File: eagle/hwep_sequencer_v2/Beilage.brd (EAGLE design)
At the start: 256.5 x 87.6 mm, 175 parts, among them X1 ESP32-AZDEL

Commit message: Board: Bedruck Formatiert
Board Optimiert und Layer:
Names
Values
Formatiert
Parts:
- moved R14 6.35 mm to (158.8, 55.9), turned to 90 degrees
- moved C15 4.07 mm to (220.3, 71.1)
- moved R49 2.84 mm to (171.4, 44.5), turned to 270 degrees
- moved R18 1.27 mm to (238.8, 26.7)
- moved R20 1.27 mm to (243.8, 26.7)
- moved R35 1.27 mm to (212.1, 49.5)
- moved R36 1.27 mm to (212.1, 44.5)
- moved R37 1.27 mm to (212.1, 57.1)
- moved R38 1.27 mm to (212.1, 52.1)
- moved R39 1.27 mm to (212.1, 47.0)
- moved R40 1.27 mm to (212.1, 62.2)
- moved R41 1.27 mm to (212.1, 54.6)
- moved R42 1.27 mm to (212.1, 59.7)
- moved R43 1.27 mm to (207.0, 43.2)
- moved R19 1.27 mm to (241.3, 26.7)
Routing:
- net GND: track 62.3 -> 76.5 mm, vias 17 -> 16
- net 7SEG_D: track 20.8 -> 24.6 mm
- net PAUSE_CNT: track 16.6 -> 12.9 mm, vias 1 -> 0
- net +3V3: track 1202.1 -> 1199.7 mm
- net CLRR: track 35.8 -> 34.2 mm
- net RESET_CNT: track 58.5 -> 59.9 mm
- net 7SEG_B: track 16.5 -> 17.8 mm
- net N$80: track 35.1 -> 33.9 mm
- net N$78: track 47.4 -> 46.1 mm
- net N$7: track 27.5 -> 26.2 mm
- net N$56: track 35.1 -> 33.9 mm
- net N$37: track 27.5 -> 26.2 mm
- net N$36: track 27.5 -> 26.2 mm
- net N$35: track 35.1 -> 33.9 mm
- net EC11_SW: track 58.4 -> 59.6 mm
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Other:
- board text added: "3x"

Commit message: Board Prototyp Fertiggestellt
Fehlende Entkoppel-Kondensatoren eingefügt
Bestückungsdruck überarbeitet und Formatiert
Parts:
- added C21, C22, C25, C26: 1u, rcl_GruS:C0805
- added C23, C24, C27, C28: 100n, rcl_GruS:C0805
- C13, C14, C17, C18: value 1u -> 100n
- R13: value 10k -> 56k; device rcl_GruS:P160L -> rcl_GruS:R0805
- R2: device rcl_GruS:R0805 -> rcl_GruS:P160L
- R20: value 56k -> 10k
- R6: value 10k -> 330R; device rcl_GruS:P160L -> rcl_GruS:R0805
- R8: value 330R -> 1M
- R9: value 1M -> 10k; device rcl_GruS:R0805 -> rcl_GruS:P160L
- moved R2 229.2 mm to (11.4, 8.89), turned to 0 degrees
- moved R8 161.3 mm to (172.7, 67.3)
- moved R7 161.3 mm to (11.4, 71.1), turned to 180 degrees
- moved R6 118.7 mm to (172.7, 72.4)
- moved R17 108.7 mm to (238.8, 26.7), turned to 90 degrees
- moved R9 99.1 mm to (92.7, 8.89), turned to 0 degrees
- moved R1 76.9 mm to (234.9, 59.7)
- moved R20 75.2 mm to (168.9, 20.3), turned to 180 degrees
- moved C15 73.4 mm to (194.3, 2.54), flipped to the bottom, turned to 0 degrees
- moved C14 71.2 mm to (208.3, 7.62), flipped to the bottom, turned to 315 degrees
- moved C16 71.0 mm to (180.3, 7.62), flipped to the bottom, turned to 45 degrees
- moved C17 57.4 mm to (175.3, 21.6), flipped to the bottom, turned to 90 degrees
- moved C18 57.2 mm to (180.3, 35.6), flipped to the bottom, turned to 135 degrees
- moved C13 52.1 mm to (213.4, 21.6), flipped to the bottom, turned to 270 degrees
- moved R13 47.3 mm to (158.8, 55.9), flipped to the bottom, turned to 90 degrees
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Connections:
- net +3V3: now also C21.1, C22.1, C23.1, C24.1, C25.1, C26.1, C27.1, C28.1, R17.2, R2.3, R9.3; no longer C13.1, C14.1, C15.1, C16.1, C17.1, C18.1, C19.1, C20.1, R13.3, R2.2, R6.3
- net +5V: now also C13.1, C14.1, C15.1, C16.1, C17.1, C18.1, C19.1, C20.1
- net 088S052_!CS!: now also R20.1; no longer R1.1
- net 23S08_!CS: now also R1.1; no longer R2.1
- net ADC0: now also R2.2; no longer R3.2
- net ADC1: now also R3.2; no longer R4.2
- net ADC2: now also R4.2; no longer R5.2
- net ADC3: now also R5.2; no longer R6.2
- net ADC4: now also R9.2; no longer R10.2
- net ADC5: now also R10.2; no longer R11.2
- net ADC6: now also R11.2; no longer R12.2
- net ADC7: now also R12.2; no longer R13.2
- net CLRR: now also R16.2; no longer R17.2
- net EC11_A: now also R17.1; no longer R18.1
- net EC11_B: now also R18.1; no longer R19.1
- net EC11_SW: now also R19.1; no longer R20.1
- net EVENT: now also R15.2, R8.2; no longer R16.2, R9.2
- net GND: now also C21.2, C22.2, C23.2, C24.2, C25.2, C26.2, C27.2, C28.2, R2.1, R7.1; no longer R17.1, R6.1
- net N$58: now also R6.2; no longer R7.2
- net N$60: now also R6.1; no longer R7.1
- net N$9: now also R7.2; no longer R8.2
- net PAUSE_CNT: now also R13.2; no longer R14.2
- net RESET_CNT: now also R14.2; no longer R15.2
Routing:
- net GND: track 76.5 -> 104.7 mm
- net +5V: track 160.6 -> 187.0 mm
- net PL_DIN: track 48.9 -> 50.1 mm
- net +3V3: track 1199.7 -> 1198.5 mm
- net N$8: track 3.37 -> 2.87 mm

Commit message: RGB Ring now in SMD
SMD RGB LEDS WS2812 used because of availability
PSU Buck Converter 12v to 5v still to be added to the schematic
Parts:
- added C29, C30: 1u, rcl_GruS:C0805
- added C31, C32: 100n, rcl_GruS:C0805
- added H46, H47, H48, H49: ge, led_GruS:LED5MM
- C21, C22: value 1u -> 100n
- H10, H3, H4, H5, H6, H7, H8, H9: value PL9823-F5 -> WS2812B; device led_GruS:LED-PL9823-F5 -> led_GruS:WS2812B
- H11, H12, H13: value (none) -> WS2812B; device display_GruS:HDSP-E -> led_GruS:WS2812B
- H14: value rt -> WS2812B; device led_GruS:CHIPLED_1206 -> led_GruS:WS2812B
- H15, H16, H17: value rt -> (none); device led_GruS:CHIPLED_1206 -> display_GruS:HDSP-E
- H30, H31, H32, H33: value gn -> rt; device led_GruS:LED5MM -> led_GruS:CHIPLED_1206
- H38, H39, H40, H41: value ge -> gn
- moved H2 225.7 mm to (236.2, 88.9)
- moved R7 225.3 mm to (236.2, 86.4)
- moved H30 200.5 mm to (205.7, 83.8)
- moved H31 183.3 mm to (208.3, 83.8)
- moved C25 173.0 mm to (212.1, 80.0), turned to 0 degrees
- moved H32 166.3 mm to (210.8, 83.8)
- moved H33 149.4 mm to (213.4, 83.8)
- moved C26 146.4 mm to (181.6, 80.0)
- moved H34 81.5 mm to (11.4, 40.6)
- moved H35 81.5 mm to (31.8, 40.6)
- moved H36 81.5 mm to (52.1, 40.6)
- moved H42 81.5 mm to (11.4, 52.1)
- moved H43 81.5 mm to (31.8, 52.1)
- moved H44 81.5 mm to (52.1, 52.1)
- moved H37 81.5 mm to (72.4, 40.6)
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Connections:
- new net N$67: H12.2, H4.4
- new net N$69: H5.2, H8.4
- new net N$71: H11.4, H8.2
- new net N$72: H11.2, H14.4
- net +3V3: now also C29.1, C30.1, C31.1, C32.1, H46.A, H47.A, H48.A, H49.A; no longer C21.1, C22.1, C23.1, C24.1, H14.A, H15.A, H16.A, H17.A
- net +5V: now also C21.1, C22.1, C23.1, C24.1, H10.1, H11.1, H12.1, H13.1, H14.1, H3.1, H4.1, H5.1, H6.1, H7.1, H8.1, H9.1; no longer H10.2, H3.2, H4.2, H5.2, H6.2, H7.2, H8.2, H9.2
- net GND: now also C29.2, C30.2, C31.2, C32.2, H11.3, H12.3, H13.3, H14.3
- net N$10: now also H18.C; no longer H14.C
- net N$11: now also H19.C; no longer H15.C
- net N$12: now also H20.C; no longer H16.C
- net N$13: now also H21.C; no longer H17.C
- net N$20: now also H22.C; no longer H18.C
- net N$21: now also H23.C; no longer H19.C
- net N$22: now also H24.C; no longer H20.C
- net N$23: now also H25.C; no longer H21.C
- net N$25: now also H26.C; no longer H22.C
- net N$26: now also H27.C; no longer H23.C
- net N$27: now also H28.C; no longer H24.C
- net N$28: now also H29.C; no longer H25.C
- net N$29: now also H30.C; no longer H26.C
- net N$30: now also H31.C; no longer H27.C
- net N$31: now also H32.C; no longer H28.C
- net N$32: now also H33.C; no longer H29.C
- net N$33: now also H15.G, H16.G, H17.G; no longer H11.G, H12.G, H13.G
- net N$35: now also H15.F, H16.F, H17.F; no longer H11.F, H12.F, H13.F
- net N$36: now also H15.A, H16.A, H17.A; no longer H11.A, H12.A, H13.A
- net N$37: now also H15.B, H16.B, H17.B; no longer H11.B, H12.B, H13.B
- net N$38: now also H34.K; no longer H30.K
- net N$39: now also H35.K; no longer H31.K
- net N$4: now also H13.2, H5.4; no longer H4.1, H9.4
- net N$40: now also H36.K; no longer H32.K
- net N$41: now also H37.K; no longer H33.K
- net N$42: now also H38.K; no longer H34.K
- net N$43: now also H39.K; no longer H35.K
- net N$44: now also H40.K; no longer H36.K
- net N$45: now also H41.K; no longer H37.K
- net N$46: now also H42.K; no longer H38.K
- net N$47: now also H43.K; no longer H39.K
- net N$48: now also H44.K; no longer H40.K
- net N$49: now also H45.K; no longer H41.K
- net N$50: now also H46.K; no longer H42.K
- net N$51: now also H47.K; no longer H43.K
- net N$52: now also H48.K; no longer H44.K
- net N$53: now also H49.K; no longer H45.K
- net N$55: now also H15.CC1, H15.CC2; no longer H11.CC1, H11.CC2
- net N$56: now also H15.D, H16.D, H17.D; no longer H11.D, H12.D, H13.D
- net N$57: now also H4.2, H7.4; no longer H4.4, H6.1
- net N$59: now also H10.4, H7.2; no longer H6.4, H8.1
- net N$63: now also H10.2, H13.4; no longer H10.1, H8.4
- net N$64: now also H16.CC1, H16.CC2; no longer H12.CC1, H12.CC2
- net N$65: now also H17.CC1, H17.CC2; no longer H13.CC1, H13.CC2
- net N$68: now also H3.2, H6.4; no longer H3.4, H5.1
- net N$7: now also H15.DP, H16.DP, H17.DP; no longer H11.DP, H12.DP, H13.DP
- net N$70: now also H6.2, H9.4; no longer H5.4, H7.1
- net N$73: now also H12.4, H9.2; no longer H7.4, H9.1
- net N$78: now also H15.C, H16.C, H17.C; no longer H11.C, H12.C, H13.C
- net N$8: now also H3.4; no longer H3.1
- net N$80: now also H15.E, H16.E, H17.E; no longer H11.E, H12.E, H13.E
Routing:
- net PL_DIN: track 50.1 -> 3.79 mm
- net N$8: track 2.87 -> 32.5 mm
- net GND: track 104.7 -> 75.8 mm
- net +3V3: track 1198.5 -> 1223.8 mm, vias 15 -> 14
- net +5V: track 187.0 -> 208.5 mm, vias 0 -> 1
- net 088S052_!CS!: track 70.4 -> 77.4 mm, vias 2 -> 0
- net N$69: track 0.00 -> 5.87 mm
- net N$71: track 0.00 -> 5.84 mm
- net N$67: track 0.00 -> 5.84 mm
- net SCK: track 162.9 -> 168.6 mm
- net N$72: track 0.00 -> 5.57 mm
- net EC11_SW: track 59.6 -> 55.6 mm, vias 1 -> 0
- net MISO: track 85.3 -> 89.2 mm
- net N$9: track 2.87 -> 0.00 mm
- net ADC4: track 74.9 -> 72.4 mm
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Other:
- board size 256.5 x 87.6 mm -> 251.5 x 94 mm

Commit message: Major Prescaler Update
Optimized Prescaler:
Now Fully Software side.
Inputs are priority encoded and put on MCP23S08 free input pins.
Issues:
Analog Reference Voltage Needed?
Dedicated PSU / Voltage converter
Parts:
- removed C31, C32: 100n, rcl_GruS:C0805
- removed D14, D16: 74AHC1G04DBV, 74xx_GruS:SOT23-5
- removed D15: STP16CP05TTR, ic_GruS:TSSOP24
- removed R14, R18: 56k, rcl_GruS:R0805
- removed R2, R9: 10k, rcl_GruS:P160L
- removed R35, R36, R37, R38, R39, R40, R41, R42: 100R, rcl_GruS:R0805
- removed R43, R44, R45: 100k, rcl_GruS:R0805
- removed R46, R48: 10k, rcl_GruS:R0805
- removed R47, R49: 2k7, rcl_GruS:R0805
- removed V10, V11, V12, V13, V14, V15, V16, V17, V18, V19, V20, V21, V22, V23, V24, V25, V4, V5, V6, V7, V8, V9: 1N4148-7, diode_GruS:DO35-7
- removed V26, V27, V28: NTR4003, mfet_GruS:SOT23
- C10, C11, C25, C26, C29, C30: value 1u -> 100n
- C23, C24, C27, C28: value 100n -> 1u
- C4, C5: value 100n -> 10n
- C6, C7: value 10n -> 100n
- D1: value 74AHC138N -> MCP23S08SO; device 74xx_GruS:DIP16 -> ic_GruS:SO18W
- D10: value 74HC73N -> STP16CP05TTR; device 74xx_GruS:DIP14 -> ic_GruS:TSSOP24
- D11: value 74HC151N -> 74AHC1G04DBV; device 74xx_GruS:DIP16 -> 74xx_GruS:SOT23-5
- D12: value 74AHCT1G125DBV -> STP16CP05TTR; device 74xx_GruS:SOT23-5 -> ic_GruS:TSSOP24
- D13: value STP16CP05TTR -> 74AHC1G04DBV; device ic_GruS:TSSOP24 -> 74xx_GruS:SOT23-5
- D2: value MCP23S08SO -> 74AHC1G125DBV; device ic_GruS:SO18W -> 74xx_GruS:SOT23-5
- D4: value 74AHC1G125DBV -> 74AHC138N; device 74xx_GruS:SOT23-5 -> 74xx_GruS:DIP16
- D6: value 74HC151N -> 74HC148N
- D7: value 74HC193D -> 74HC148N; device 74xx_GruS:SO16 -> 74xx_GruS:DIP16
- D8: value 74HC73N -> 74HC00N
- D9: value 74HC73N -> 74AHCT1G125DBV; device 74xx_GruS:DIP14 -> 74xx_GruS:SOT23-5
- R13: value 56k -> 10k; device rcl_GruS:R0805 -> rcl_GruS:P160L
- R15, R16, R17, R19: value 56k -> 10k
- R20: value 10k -> 100R
- R21, R22, R23, R24, R25, R26, R27: value 100k -> 100R
- R31, R33: value 100k -> 10k
- R32, R34: value 100k -> 2k7
- R6: value 330R -> 10k; device rcl_GruS:R0805 -> rcl_GruS:P160L
- R7: value 330R -> 1k
- R8: value 1M -> 1k
- S14: value (none) -> EC11E09244AQ; device switch_GruS:B3F-10XX -> switch_GruS:EC11
- S15: value EC11E09244AQ -> (none); device switch_GruS:EC11 -> switch_GruS:B3F-10XX
- V2, V3: value 1N4148-7 -> NTR4003; device diode_GruS:DO35-7 -> mfet_GruS:SOT23
- moved R32 205.8 mm to (227.3, 78.7), turned to 0 degrees
- moved R21 201.2 mm to (212.1, 50.8), turned to 180 degrees
- moved R28 198.6 mm to (207.0, 49.5), turned to 0 degrees
- moved R22 188.0 mm to (212.1, 63.5), turned to 180 degrees
- moved R27 185.4 mm to (212.1, 66.0), turned to 180 degrees
- moved C27 179.6 mm to (42.5, 52.1)
- moved R29 177.3 mm to (198.1, 49.5), turned to 0 degrees
- moved R31 176.5 mm to (221.0, 83.8), flipped to the top
- moved C28 173.5 mm to (42.5, 40.6), turned to 180 degrees
- moved R23 170.4 mm to (212.1, 58.4), turned to 180 degrees
- moved R24 168.1 mm to (212.1, 53.3), turned to 180 degrees
- moved R30 145.1 mm to (188.0, 49.5), turned to 0 degrees
- moved R34 133.7 mm to (171.4, 50.8), flipped to the top
- moved D9 130.8 mm to (242.6, 21.6)
- moved R25 129.6 mm to (212.1, 68.6), turned to 180 degrees
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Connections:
- removed net !CS!_C: D1.3, X1.36
- removed net BPM_DIV_Q0: D6.11, D9.9
- removed net BPM_DIV_Q1: D10.12, D6.10
- removed net BPM_DIV_Q2: D10.9, D6.9
- removed net GATE_DIV_Q0: D11.11, D8.9
- removed net GATE_DIV_Q1: D11.10, D8.12
- removed net GATE_DIV_Q2: D11.9, D9.12
- removed net N$14: D8.3, R25.2, V6.C, V9.C
- removed net N$15: D9.10, R30.2, V14.C, V16.C
- removed net N$16: D10.10, R34.2, V23.C, V24.C, V25.C
- removed net N$17: D10.7, R33.2, V22.C
- removed net N$18: D10.14, R31.2, V19.C, V20.C
- removed net N$19: D9.7, R29.2, V15.C, V17.C
- removed net N$2: D8.10, R23.2, V2.C, V4.C
- removed net N$3: D8.14, R24.2, V7.C, V8.C
- removed net N$34: D10.3, R32.2, V18.C, V21.C
- removed net N$5: D8.7, R22.2, V3.C, V5.C
- removed net N$6: D9.3, R27.2, V11.C, V12.C, V13.C
- removed net N$60: R6.1, V1.3
- removed net PS_BPM: D6.5, X1.6
- removed net PS_GATE: D11.5, X1.5
- removed net Q0: D11.3, D6.3, D7.3
- removed net Q1: D11.2, D6.2, D7.2
- removed net Q2: D11.1, D6.1, D7.6
- removed net Q3: D11.15, D6.15, D7.7
- removed net SRC_BPM: D10.1, D10.5, D11.4, D6.4, D7.4, D8.1, D8.5, D9.1, D9.5, X1.7
- new net AGND: C6.2, D5.3, R10.1, R11.1, R12.1, R13.1, R3.1, R4.1, R5.1, R6.1
- new net GS_B: D6.14, D8.13
- new net GS_G: D7.14, D8.12
- new net PS0: D1.14, D8.3
- new net PS1: D1.15, D8.6
- new net PS2: D1.16, D8.8
- new net PS3: D1.17, D8.11
- new net PS_B0: D6.9, D8.1
- new net PS_B1: D6.7, D8.4
- new net PS_B2: D6.6, D8.10
- new net PS_G0: D7.9, D8.2
- new net PS_G1: D7.7, D8.5
- new net PS_G2: D7.6, D8.9
- net !CS!_A: now also D4.1; no longer D1.1
- net !CS!_B: now also D4.2; no longer D1.2
- net +3V3: now also C23.1, C24.1, C6.1, C7.1, D1.18, D10.24, D11.5, D12.24, D13.5, D2.5, D4.16, D4.6, D6.10, D6.11, D6.12, D7.10, D7.12, D8.14, R13.3, R15.2, R16.2, R31.2, R33.2, R6.3, S14.C1; no longer C10.1, C11.1, C31.1, C32.1, C4.1, C5.1, D1.16, D10.4, D11.16, D13.24, D14.5, D15.24, D16.5, D2.18, D2.6, D4.5, D7.5, D8.4, D9.4, H1.A, R18.2, R2.3, R20.2, R21.2, R28.2, R46.2, R48.2, R9.3, S10.2, S11.1, S12.1, S13.2, S14.1, S2.1, S3.1, S4.1, S5.1, S7.2, S8.2, S9.2
- net +5V: now also C10.1, C11.1, D9.5; no longer C23.1, C24.1, D12.5
- net 088S052_!CS!: now also D4.12, R19.1; no longer D1.12, R20.1
- net 23S08_!CS: now also D1.7, D2.1, D4.15; no longer D1.15, D2.7, D4.1
- net 7SEG_A: now also R27.2; no longer R42.2
- net 7SEG_B: now also R26.2; no longer R41.2
- net 7SEG_C: now also R25.2; no longer R40.2
- net 7SEG_CE: now also R30.2, V3.1; no longer R45.2, V28.1
- net 7SEG_CH: now also R28.2, V1.1; no longer R43.2, V26.1
- net 7SEG_CZ: now also R29.2, V2.1; no longer R44.2, V27.1
- net 7SEG_D: now also R24.2; no longer R39.2
- net 7SEG_DP: now also R20.2; no longer R35.2
- net 7SEG_E: now also R23.2; no longer R38.2
- net 7SEG_F: now also R22.2; no longer R37.2
- net 7SEG_G: now also R21.2; no longer R36.2
- net ADC0: now also R3.2; no longer R2.2
- net ADC1: now also R4.2; no longer R3.2
- net ADC2: now also R5.2; no longer R4.2
- net ADC3: now also R6.2; no longer R5.2
- net ADC4: now also R10.2; no longer R9.2
- net ADC5: now also R11.2; no longer R10.2
- net ADC6: now also R12.2; no longer R11.2
- net ADC7: now also R13.2; no longer R12.2
- net CLRR: now also D1.11; no longer D2.11, R16.2
- net EC11_A: now also C4.1, R15.1, S14.A1; no longer C6.1, R17.1, S15.A1
- net EC11_B: now also C5.1, R16.1, S14.B1; no longer C7.1, R18.1, S15.B1
- net EC11_SW: now also R17.1, S14.E1; no longer R19.1, S15.E1
- net EVENT: now also D1.10, H1.A, S12.4; no longer D2.10, R15.2, R8.2, S13.4, V1.1
- net GND: now also D1.9, D10.1, D10.21, D11.3, D12.21, D13.3, D2.3, D4.4, D4.5, D4.8, D6.5, D8.7, D9.1, D9.3, R28.1, S1.2, S10.1, S10.2, S11.1, S11.2, S12.1, S12.2, S13.1, S13.2, S14.D1, S14.MH1, S14.MH2, S15.1, S15.2, S2.1, S2.2, S3.1, S3.2, S4.1, S4.2, S5.1, S5.2, S6.2, S7.1, S7.2, S8.1, S8.2, S9.1, S9.2, V2.2, V3.2; no longer C31.2, C32.2, C6.2, D1.8, D10.11, D11.7, D11.8, D12.3, D13.1, D13.21, D14.3, D15.1, D15.21, D16.3, D2.4, D2.5, D2.9, D4.3, D5.3, D6.7, D7.14, D8.11, D9.11, R10.1, R11.1, R12.1, R13.1, R14.1, R15.1, R16.1, R2.1, R22.1, R23.1, R24.1, R25.1, R26.1, R27.1, R3.1, R31.1, R33.1, R4.1, R43.1, R44.1, R45.1, R47.1, R49.1, R5.1, R9.1, S15.C1, S15.D1, S15.MH1, S15.MH2, V26.2, V27.2, V28.2
- net MISO: now also D2.4; no longer D4.4
- net MOSI: now also D10.2, D12.2; no longer D13.2, D15.2
- net N$1: now also D6.15, D7.5; no longer D9.14, R26.2, V10.C
- net N$10: now also D10.5; no longer D13.5
- net N$11: now also D10.6; no longer D13.6
- net N$12: now also D10.7; no longer D13.7
- net N$13: now also D10.8; no longer D13.8
- net N$20: now also D10.9; no longer D13.9
- net N$21: now also D10.10; no longer D13.10
- net N$22: now also D10.11; no longer D13.11
- net N$23: now also D10.12; no longer D13.12
- net N$24: now also D10.23, R32.2; no longer D13.23, R47.2
- net N$25: now also D10.13; no longer D13.13
- net N$26: now also D10.14; no longer D13.14
- net N$27: now also D10.15; no longer D13.15
- net N$28: now also D10.16; no longer D13.16
- net N$29: now also D10.17; no longer D13.17
- net N$30: now also D10.18; no longer D13.18
- net N$31: now also D10.19; no longer D13.19
- net N$32: now also D10.20; no longer D13.20
- net N$33: now also R21.1; no longer R36.1
- net N$35: now also R22.1; no longer R37.1
- net N$36: now also R27.1; no longer R42.1
- net N$37: now also R26.1; no longer R41.1
- net N$38: now also D12.5; no longer D15.5
- net N$39: now also D12.6; no longer D15.6
- net N$40: now also D12.7; no longer D15.7
- net N$41: now also D12.8; no longer D15.8
- net N$42: now also D12.9; no longer D15.9
- net N$43: now also D12.10; no longer D15.10
- net N$44: now also D12.11; no longer D15.11
- net N$45: now also D12.12; no longer D15.12
- net N$46: now also D12.13; no longer D15.13
- net N$47: now also D12.14; no longer D15.14
- net N$48: now also D12.15; no longer D15.15
- net N$49: now also D12.16; no longer D15.16
- net N$50: now also D12.17; no longer D15.17
- net N$51: now also D12.18; no longer D15.18
- net N$52: now also D12.19; no longer D15.19
- net N$53: now also D12.20; no longer D15.20
- net N$54: now also D12.23, R34.2; no longer D15.23, R49.2
- net N$55: now also V1.3; no longer V26.3
- net N$56: now also R24.1; no longer R39.1
- net N$58: now also R7.2; no longer R6.2
- net N$61: now also D12.4, D13.4, R33.1; no longer D15.4, D16.4, R48.1
- net N$62: now also D1.3, D2.2; no longer D2.3, D4.2
- net N$64: now also V2.3; no longer V27.3
- net N$65: now also V3.3; no longer V28.3
- net N$66: now also D10.4, D11.4, R31.1; no longer D13.4, D14.4, R46.1
- net N$7: now also R20.1; no longer R35.1
- net N$78: now also R25.1; no longer R40.1
- net N$8: now also D9.4; no longer D12.4
- net N$80: now also R23.1; no longer R38.1
- net N$9: now also R8.2; no longer R7.2
- net PAUSE_CNT: now also D1.13, S13.4; no longer D2.13, R13.2, S12.3
- net PL_DIN: now also D9.2; no longer D12.2
- net Q0_SW_BD: now also D6.3, S2.4; no longer S2.3, V17.A, V21.A, V25.A
- net Q0_SW_GD: now also D7.3; no longer V13.A, V5.A, V9.A
- net Q1_SW_BD: now also D6.2, S3.4; no longer S3.3, V16.A, V20.A, V24.A
- net Q1_SW_GD: now also D7.2; no longer V12.A, V4.A, V8.A
- net Q2_SW_BD: now also D6.1; no longer V15.A, V19.A, V23.A
- net Q2_SW_GD: now also D7.1, S9.3; no longer S9.4, V11.A, V3.A, V7.A
- net Q3_SW_BD: now also D6.13, S5.4; no longer S5.3, V14.A, V18.A, V22.A
- net Q3_SW_GD: now also D7.13; no longer V10.A, V2.A, V6.A
- net RESET_CNT: now also D1.12, S15.3; no longer D2.12, R14.2, S14.3
- net SCK: now also D1.1, D10.3, D12.3; no longer D13.3, D15.3, D2.1
- net SRC_SW_BD: now also D6.4, S1.4; no longer D10.2, D10.6, D9.6, R28.1, S1.3
- net SRC_SW_GD: now also D7.4, S6.4; no longer D8.2, D8.6, D9.2, R21.1, S6.3
- net STP_LE_K: now also D11.2, D4.13; no longer D1.13, D14.2
- net STP_LE_S: now also D13.2, D4.14; no longer D1.14, D16.2
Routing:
- net SRC_BPM: track 242.4 -> 0.00 mm, vias 1 -> 0
- net +3V3: track 1223.8 -> 1005.3 mm, vias 14 -> 7
- net AGND: track 0.00 -> 149.6 mm, vias 0 -> 1
- net PS_BPM: track 124.7 -> 0.00 mm, vias 1 -> 0
- net N$19: track 115.3 -> 0.00 mm, vias 1 -> 0
- net N$6: track 107.6 -> 0.00 mm, vias 1 -> 0
- net PS_GATE: track 102.5 -> 0.00 mm, vias 1 -> 0
- net N$5: track 100.4 -> 0.00 mm
- net N$16: track 97.2 -> 0.00 mm, vias 1 -> 0
- net N$14: track 96.6 -> 0.00 mm, vias 1 -> 0
- net N$34: track 92.8 -> 0.00 mm, vias 1 -> 0
- net Q0_SW_BD: track 8.13 -> 90.3 mm
- net N$15: track 78.5 -> 0.00 mm
- net Q0_SW_GD: track 13.2 -> 90.3 mm
- net N$2: track 74.4 -> 0.00 mm
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
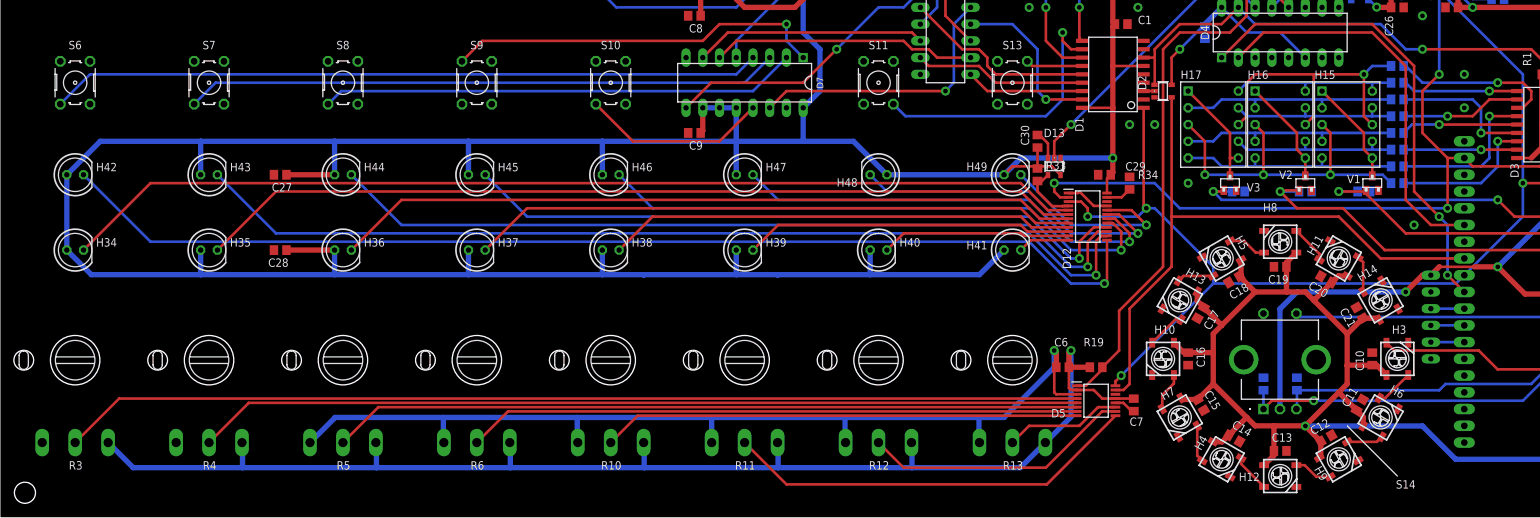
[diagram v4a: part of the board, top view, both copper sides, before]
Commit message: fixed traces
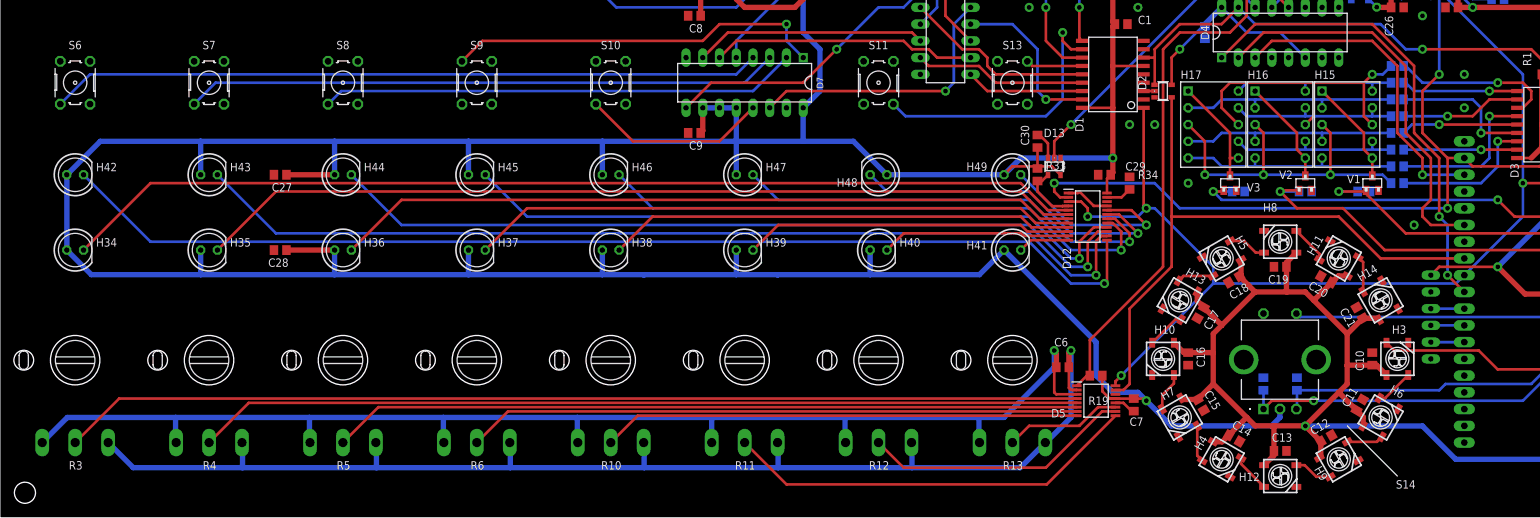
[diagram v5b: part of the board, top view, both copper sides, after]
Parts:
- moved R19 1.27 mm to (166.4, 21.6), turned to 0 degrees
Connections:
- new net !CS!_C: D4.3, X1.36
- new net VREF: C6.1, D5.2, R10.3, R11.3, R12.3, R13.3, R3.3, R4.3, R5.3, R6.3
- net +3V3: no longer C6.1, D5.2, R10.3, R11.3, R12.3, R13.3, R3.3, R4.3, R5.3, R6.3
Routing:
- net VREF: track 0.00 -> 191.2 mm, vias 0 -> 1
- net +3V3: track 1005.3 -> 829.1 mm, vias 7 -> 6
- net !CS!_C: track 0.00 -> 48.7 mm, vias 0 -> 1
- net AGND: track 149.6 -> 197.9 mm
- net N$78: track 46.1 -> 47.2 mm
- net !CS!_B: track 59.9 -> 60.9 mm
- net 088S052_!CS!: track 82.6 -> 82.0 mm

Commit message: Documentation Update
Added STL
cleaned up docs
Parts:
- R10, R11, R12, R13, R3, R4, R5, R6: device rcl_GruS:P160L -> rcl_GruS:P160LB
- X1: value ESP32-AZDEL -> ESP32-DEVKIT-C; device modul_GruS:ESP32-AZDEL -> modul_GruS:ESP32-DEVKIT-C
- moved C6 3.59 mm to (163.8, 25.4), turned to 90 degrees
- turned H48 to 0 degrees
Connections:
- net +3V3: no longer S14.C1
- net 7SEG_CE: now also R28.2, V1.1, X1.10; no longer R30.2, V3.1, X1.8
- net 7SEG_CH: now also R30.2, V3.1, X1.8; no longer R28.2, V1.1, X1.10
- net GND: now also S14.C1
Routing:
- net +3V3: track 829.1 -> 879.4 mm, vias 6 -> 8
- net 7SEG_CH: track 54.1 -> 72.3 mm
- net 7SEG_CE: track 72.3 -> 54.1 mm
- net VREF: track 191.2 -> 187.8 mm
- net +5V: track 208.5 -> 205.2 mm, vias 1 -> 2
- net N$52: track 50.2 -> 47.7 mm
- net Q2_SW_GD: track 57.7 -> 56.2 mm
- net AGND: track 197.9 -> 197.1 mm
- net GND: vias 15 -> 16
